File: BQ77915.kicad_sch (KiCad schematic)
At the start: 1 part, among them U1 BQ7791500PWR

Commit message: added SA balancer design (WiP)
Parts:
- added BT4, BT5, BT6: Battery_Cell, Inductor Wuerth:BAT_1043, symbol Device:Battery_Cell
- added C30, C31, C32, C33: C_IN, symbol Device:C
- added C34, C35: C_VDD, symbol Device:C
- added C36, C37, C38: C_S, symbol Device:C
- added D13, D4, D6: D, symbol Device:D
- added Q5, Q6: NMOS, symbol Simulation_SPICE:NMOS
- added R10, R13, R18, R19: R_IN, symbol Device:R
- added R22: R_HIB, symbol Device:R
- added R25: R_TS_PU, symbol Device:R
- added R27: R_OCD, symbol Device:R
- added R28: R_LD, symbol Device:R
- added R29: R_CHG, symbol Device:R
- added R30: R_CHG2, symbol Device:R
- added R31, R33: R_GS, symbol Device:R
- added R36: R_DSG, symbol Device:R
- added R37: R_SNS, symbol Device:R
- added R38, R39: R_S, symbol Device:R
- added R8: R_VDD, symbol Device:R
- added TH2: R_TS, symbol Device:Thermistor
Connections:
- net at U1.1 (VDD): now also C34.1, R8.2
- net at U1.2 (AVDD): now also C35.1
- net GND: now reaches U1.9 (VSS)
- net GND: now also U1.16 (CBI), U1.20 (CCFG), U1.23 (CTRC), U1.24 (CTRD), BT6.N (-), C32.2, C33.1, C34.2, C35.2, C36.2, C37.2, R19.2, R27.1, R37.1, R38.2, TH2.2
- net at U1.10 (SRP): now also C36.1, C38.1, R38.1
- net at U1.11 (SRN): now also C37.1, C38.2, R39.1
- net at U1.12 (DSG): now also R36.1
- net at U1.13 (CHG): now also R29.1
- net at U1.14 (LD): now also R28.2
- net at U1.17 (OCDP): now also R27.2
- net at U1.18 (TS): now also R25.2, TH2.1
- net at U1.19 (VTB): now also R25.1
- net at U1.22 (PRES): now also R22.2
- net BAT3: now reaches U1.3 (VC5)
- net BAT3: now also U1.4 (VC4), U1.5 (VC3), C30.1, R10.2
- net BAT2: now reaches U1.6 (VC2)
- net BAT2: now also C30.2, C31.1, R13.2
- net BAT1: now reaches U1.7 (VC1)
- net BAT1: now also C31.2, C32.1, R18.2
- net BAT0: now reaches U1.8 (VC0)
- net BAT0: now also C33.2, R19.1
- new net: D4.1 (K), Q5.2 (G), R30.2, R31.1
- new net: D4.2 (A), R29.2, R30.1
- new net: Q6.2 (G), R33.1, R36.2
- new net: D13.1 (K), D6.1 (K), Q5.1 (D), Q6.1 (D)
- new net: D13.2 (A), Q6.3 (S), R33.2, R37.2, R39.2
- new net: BT5.N (-), BT6.P (+), R18.1
- new net: BT4.N (-), BT5.P (+), R13.1
- new net PACK+: BT4.P (+), R10.1, R8.1
- new net PACK-: D6.2 (A), Q5.3 (S), R28.1, R31.2
- new net PRES: R22.1
- no-connect marks 0 -> 2
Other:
- note added: "INFO: Internal cell balancing should be used for cell balancing currents up to 50 mA. External MOSFETs have to be used if higher cell balancing currents are required"
- note added: "todo: -do we want hibernate mode? (i.e. no balancing or fault detection and low power consumption -> good for shipping mode) -this is only the schematic of the "typical application" (see 10.2 page 39). maybe we want to adjust something (take a look at 10. page 33) -do we want external balancing or internal balancing? -apparently it is possiblie to overwrite CHG or DSG driver through CTRC or CTRD 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"
- moved on the sheet: U1A, U1B

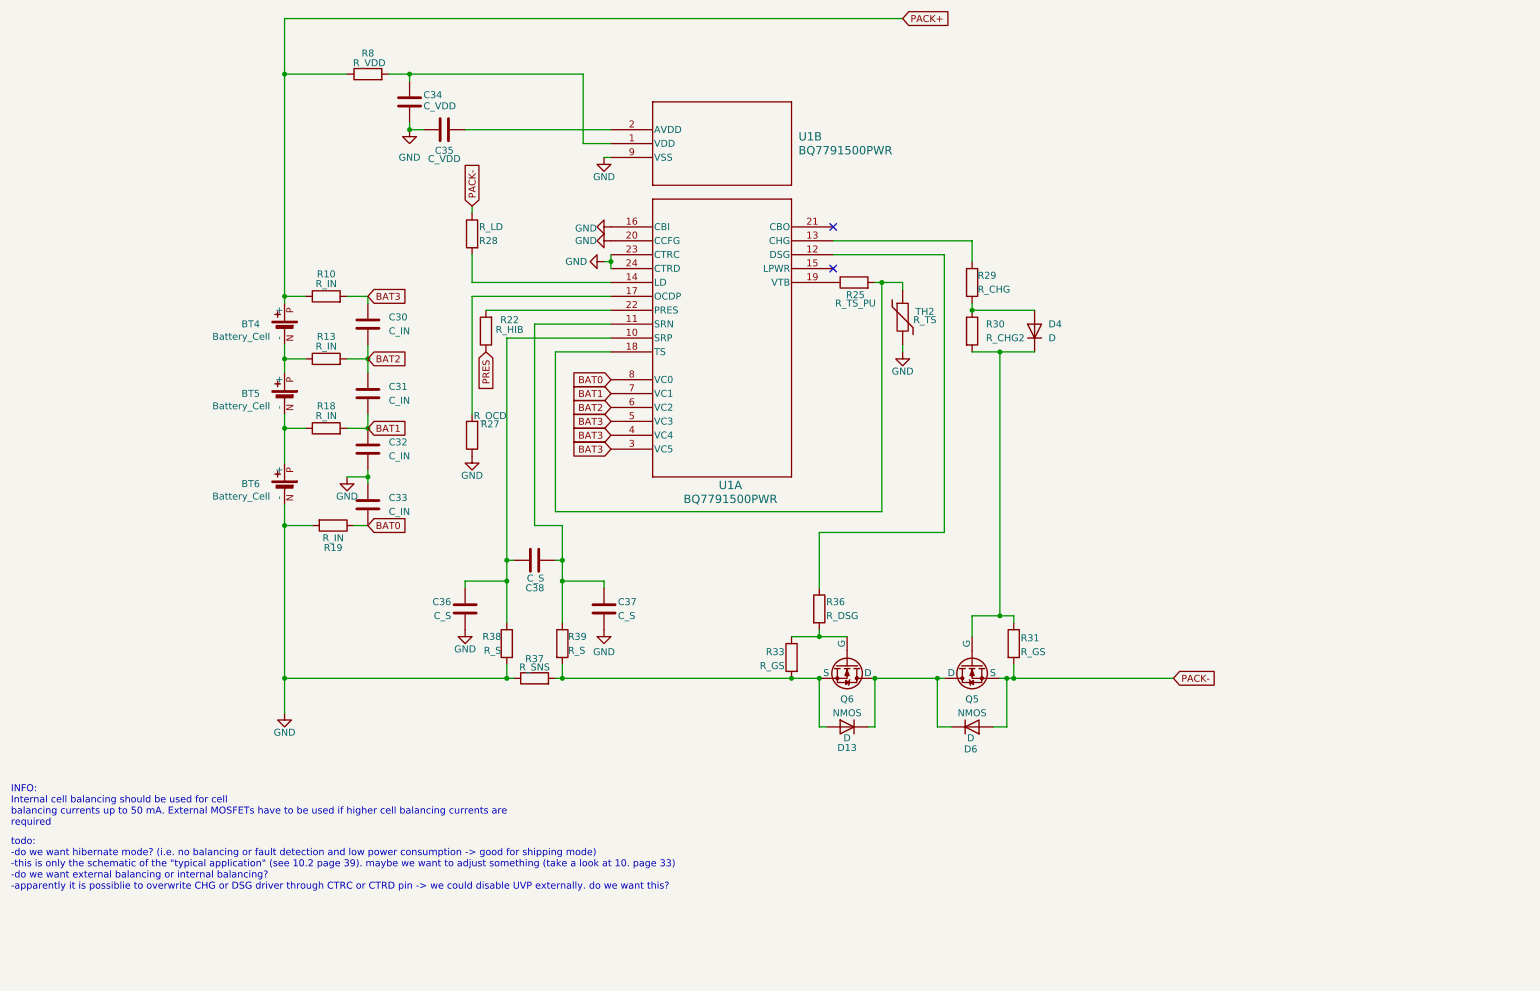
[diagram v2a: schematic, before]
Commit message: added balancer thermistor info; changed MCU pinout to support CAN bootloading
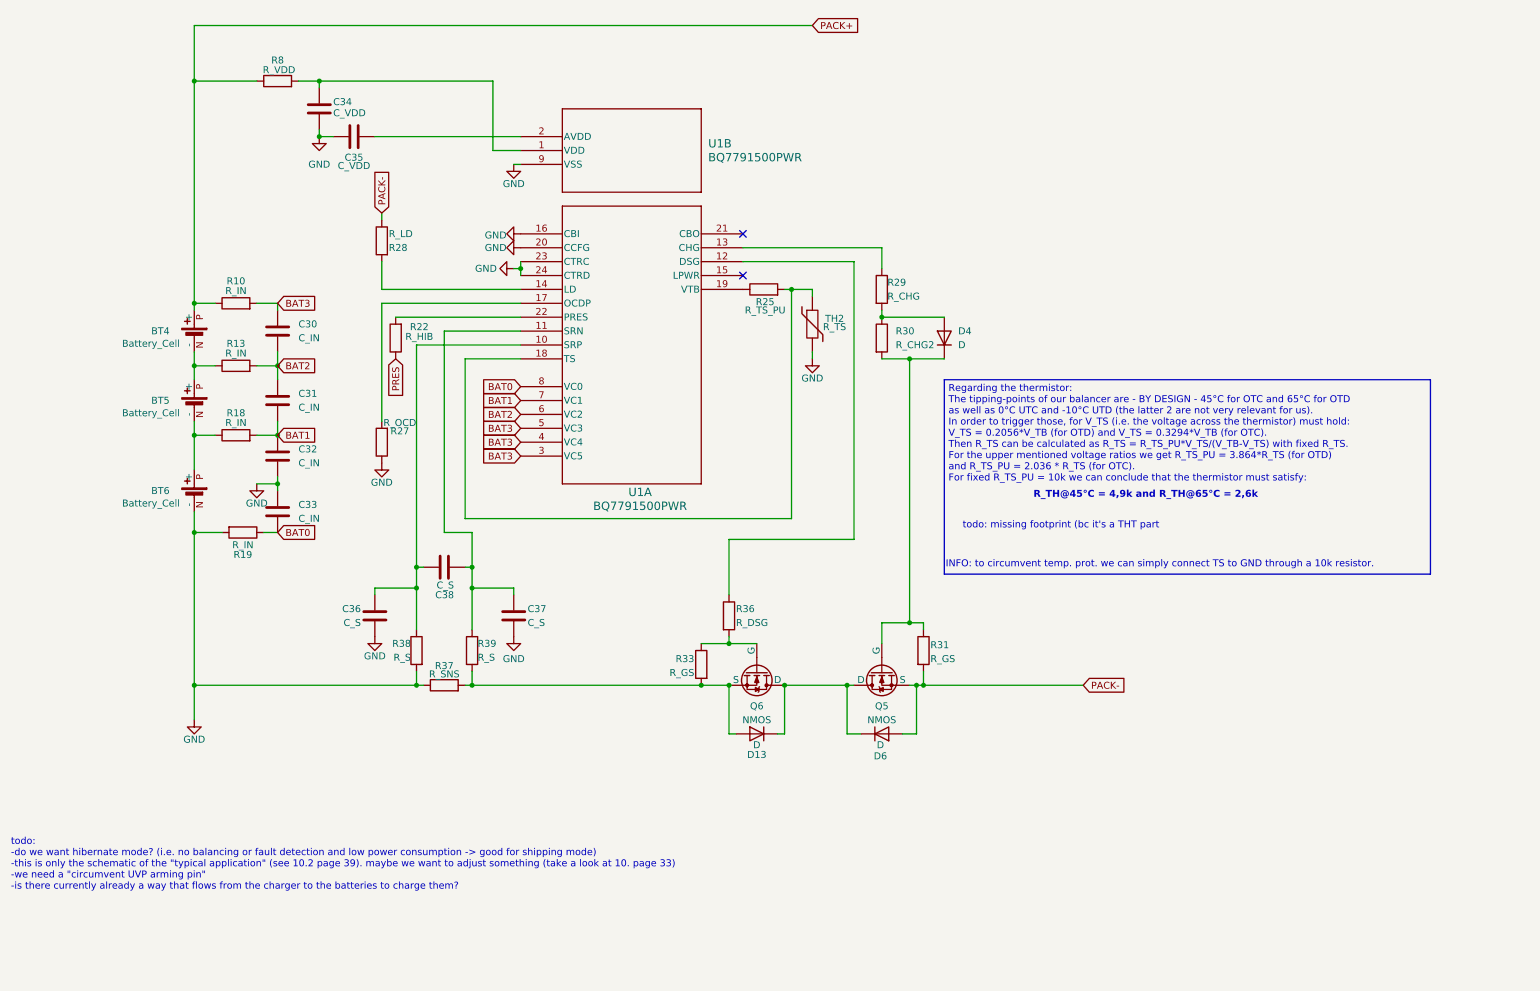
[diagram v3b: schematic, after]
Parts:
- TH2: LCSC (none) -> C84036
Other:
- note added: "INFO: to circumvent temp. prot. we can simply connect TS to GND through a 10k resistor."
- note added: "R_TH@45°C = 4,9k and R_TH@65°C = 2,6k"
- note added: "Regarding the thermistor: The tipping-points of our balancer are - BY DESIGN - 45°C for OTC and 65°C for OTD as well as 0°C UTC and -10°C UTD (the latter 2 are not very relevant for us). In order to trigger those, for V_TS (i.e. the voltage across the thermistor) must hold: V_TS = 0.2056*V_TB (for OTD) and V_TS = 0.3294*V_TB (for OTC). Then R_TS can be calculated as R_TS = R_TS_PU*V_TS/(V_TB-V_TS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"
- note added: "todo: -do we want hibernate mode? (i.e. no balancing or fault detection and low power consumption -> good for shipping mode) -this is only the schematic of the "typical application" (see 10.2 page 39). maybe we want to adjust something (take a look at 10. page 33) -we need a "circumvent UVP arming pin" -is there currently already a way that flows from the charger to the batteries to charge them?"
- note added: "todo: missing footprint (bc it's a THT part"
- note removed: "INFO: Internal cell balancing should be used for cell balancing currents up to 50 mA. External MOSFETs have to be used if higher cell balancing currents are required"
- note removed: "todo: -do we want hibernate mode? (i.e. no balancing or fault detection and low power consumption -> good for shipping mode) -this is only the schematic of the "typical application" (see 10.2 page 39). maybe we want to adjust something (take a look at 10. page 33) -do we want external balancing or internal balancing? -apparently it is possiblie to overwrite CHG or DSG driver through CTRC or CTRD 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"
- moved on the sheet: BT4, BT5, BT6, C30, C31, C32, C33, C34, C35, C36, C37, C38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

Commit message: Changed Balancer layout to support OVP, UVP and UVP-circumvention; added UVP-circumvention arming connector
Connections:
- net PACK-: no longer D6.2 (A), Q5.3 (S), R31.2
- net UVP_OVERRIDE+: now reaches D13.1 (K), D6.1 (K), Q5.1 (D), Q6.1 (D)
- net UVP_OVERRIDE-: now reaches D13.2 (A), Q6.3 (S), R33.2, R37.2, R39.2
- net GND renamed BAL_GND
- net PACK+ renamed BAT+
- new net BAT-: D6.2 (A), Q5.3 (S), R31.2
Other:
- note added: "todo: -do we want hibernate mode? (i.e. no balancing or fault detection and low power consumption -> good for shipping mode) -this is only the schematic of the "typical application" (see 10.2 page 39). maybe we want to adjust something (take a look at 10. page 33) -all grounds in tis schematic should be a different GND level (PACK_GND) that is NOT connected to the rest of the PCB's GNDs"
- note removed: "todo: -do we want hibernate mode? (i.e. no balancing or fault detection and low power consumption -> good for shipping mode) -this is only the schematic of the "typical application" (see 10.2 page 39). maybe we want to adjust something (take a look at 10. page 33) -we need a "circumvent UVP arming pin" -is there currently already a way that flows from the charger to the batteries to charge them?"

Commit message: added explanations for balancer schematic and some component values
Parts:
- C30, C31, C32, C33: value C_IN -> 100n
- C34, C35: value C_VDD -> 1u
- C36, C37, C38: value C_S -> 100n
- R33: value R_GS -> 1M
- R38, R39: value R_S -> 100
- R8: value R_VDD -> 1k
- R_HIB: renamed from R22; value R_HIB -> 10k
- R_LD: renamed from R28; value R_LD -> 450k
- R_TS_PU: renamed from R25; value R_TS_PU -> 10k
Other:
- note added: "Low Side Switching: Therefore if OV is detected, charging gets disabled by deactivating Q5. Note that current can still flow into the negative pole of the batteries via D6 (i.e. discharge is still allowed). If UV is detected, discharge gets disabled by deactivating Q6. Note that current can still flow out of the negative pole of the batteries via D13 (i.e. charging is still allowed). To circumven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"
- note added: "todo: -do we want hibernate mode? (i.e. no balancing or fault detection and low power consumption -> good for shipping mode) -all grounds in tis schematic should be a different GND level (PACK_GND) that is NOT connected to the rest of the PCB's GNDs"
- note removed: "todo: -do we want hibernate mode? (i.e. no balancing or fault detection and low power consumption -> good for shipping mode) -this is only the schematic of the "typical application" (see 10.2 page 39). maybe we want to adjust something (take a look at 10. page 33) -all grounds in tis schematic should be a different GND level (PACK_GND) that is NOT connected to the rest of the PCB's GNDs"
- moved on the sheet: D13, D6

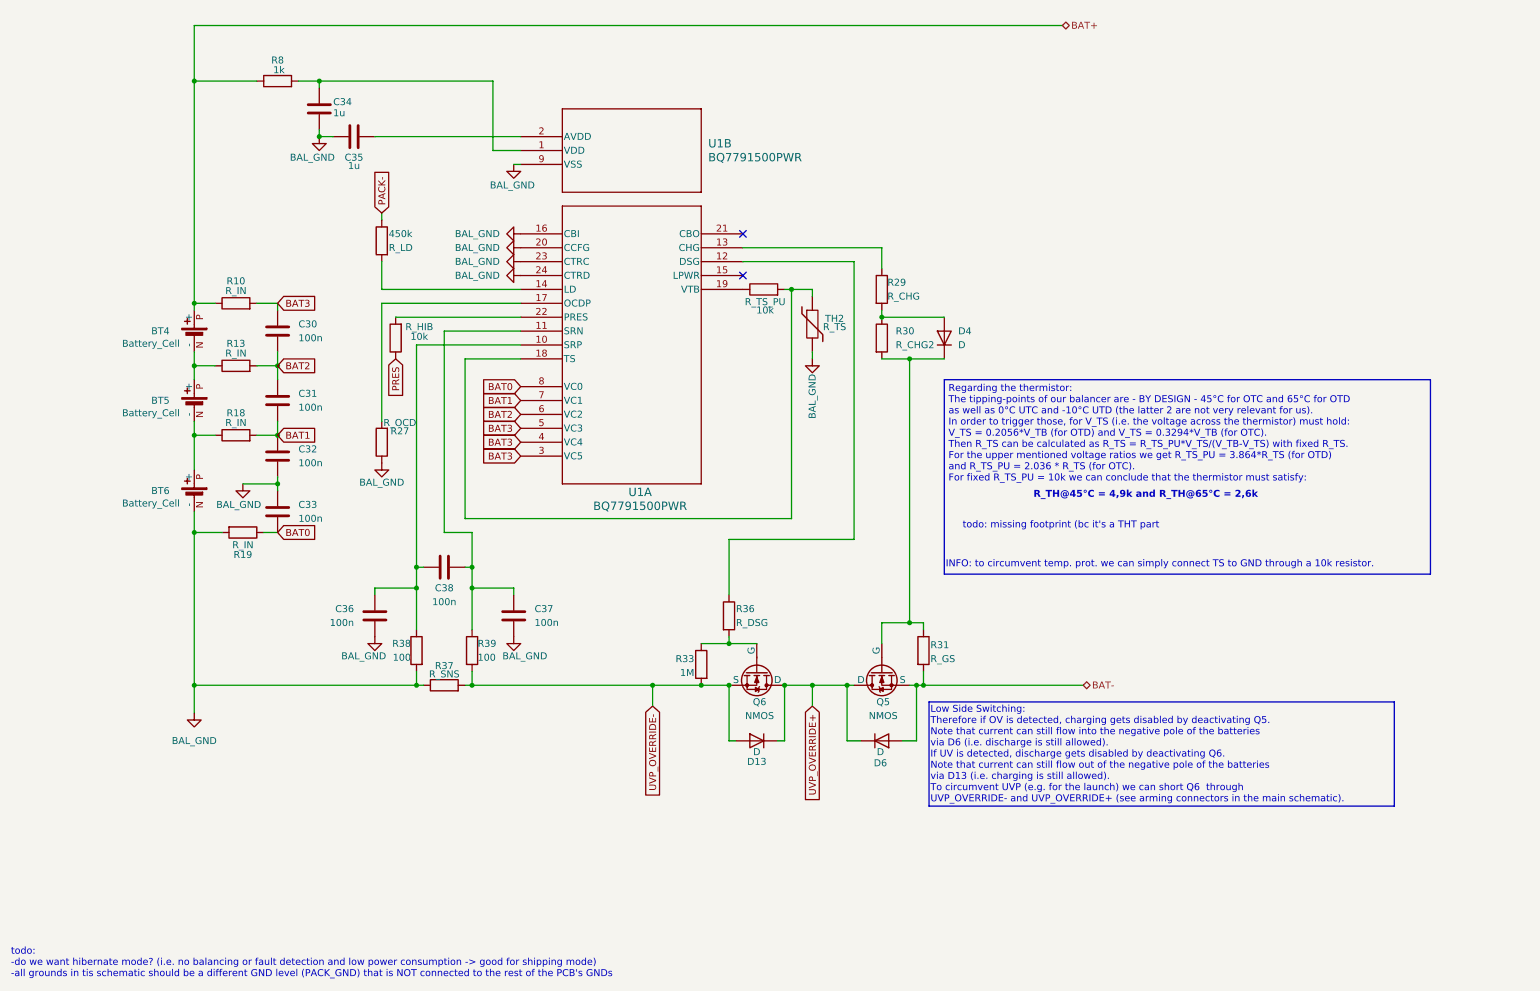
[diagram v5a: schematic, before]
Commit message: changed balancer layout according to new requirements (i.e. removed OVP/UVP, OTP/UTP, OCP/UCP); reduced arming connectors to only one
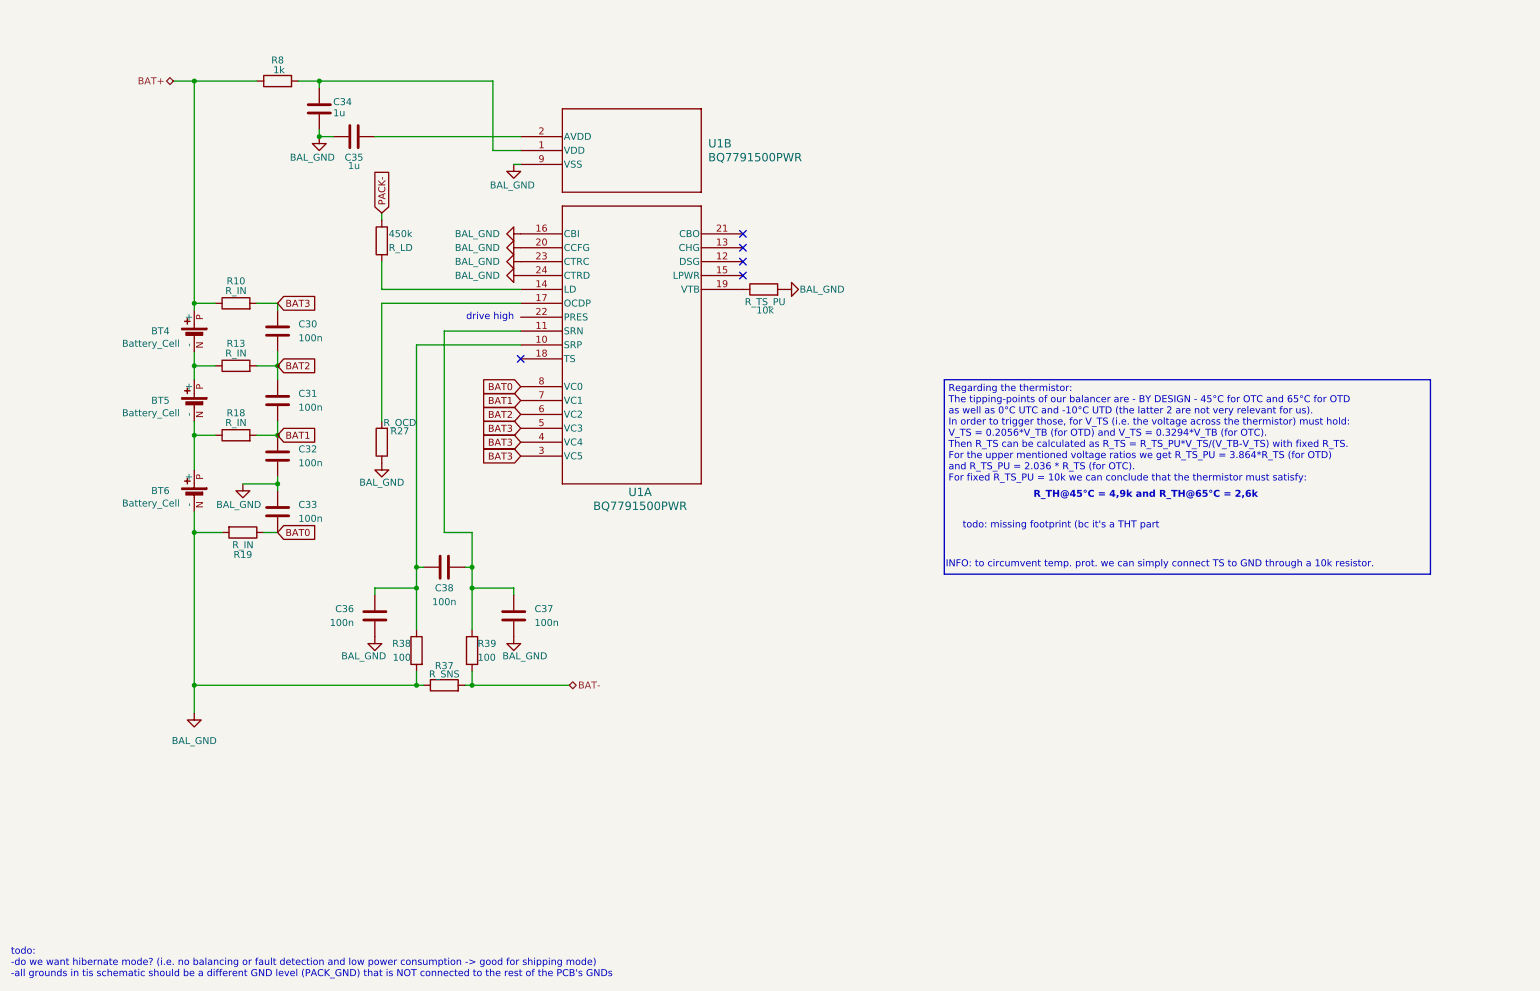
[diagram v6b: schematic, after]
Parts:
- removed D13, D4, D6: D, symbol Device:D
- removed Q5, Q6: NMOS, symbol Simulation_SPICE:NMOS
- removed R29: R_CHG, symbol Device:R
- removed R30: R_CHG2, symbol Device:R
- removed R31: R_GS, symbol Device:R
- removed R33: 1M, symbol Device:R
- removed R36: R_DSG, symbol Device:R
- removed R_HIB: 10k, symbol Device:R
- removed TH2: R_TS, symbol Device:Thermistor
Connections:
- net UVP_OVERRIDE- is gone; now on net BAT-: R37.2, R39.2
- net BAL_GND: now also R_TS_PU.2
- net at U1.18 (TS): no longer R_TS_PU.2
- no-connect marks 2 -> 5
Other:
- note added: "drive high"
- note removed: "Low Side Switching: Therefore if OV is detected, charging gets disabled by deactivating Q5. Note that current can still flow into the negative pole of the batteries via D6 (i.e. discharge is still allowed). If UV is detected, discharge gets disabled by deactivating Q6. Note that current can still flow out of the negative pole of the batteries via D13 (i.e. charging is still allowed). To circumven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"
